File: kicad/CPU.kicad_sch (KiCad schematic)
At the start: 24 parts, among them U12 GAL22V10, U16 74LS245, U17 74LS244, U18 74LS244, U19 74LS244, U20 74LS245, U3 68010P10, U4 GAL22V10, U5 SST39SF040, U6 AS6C4008-55PCN, U7 SST39SF040, U8 AS6C4008-55PCN

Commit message: Added Bus error handling
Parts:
- added J3, J4: Conn_01x01_Pin, symbol Connector:Conn_01x01_Pin
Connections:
- net at U4.1 (I0/CLK): now also J4.1 (Pin_1)
- net AS: now reaches U4.22 (I/O)
- net at U4.23 (I/O): now also J3.1 (Pin_1)
- net at R8.2, U3.12 (BGACK), U3.13 (BR)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: no longer U3.22 (BERR)
- net E: now reaches U3.20 (E)
- new net ~{BERR}: U3.22 (BERR)
- no-connect marks 22 -> 18
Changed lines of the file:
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@@
   (junction (at 275.59 25.4) (diameter 0) (color 0 0 0 0)
   )
-  (junction (at 20.32 88.9) (diameter 0) (color 0 0 0 0)
-  )
   (junction (at 265.43 236.22) (diameter 0) (color 0 0 0 0)
   )
@@
   )
   (no_connect (at 146.05 151.13))
-  (no_connect (at 40.64 77.47))
   (no_connect (at 237.49 90.17))
   (no_connect (at 212.09 87.63))
@@
   (no_connect (at 212.09 69.85))
   (no_connect (at 40.64 74.93))
-  (no_connect (at 238.76 163.83))
   (no_connect (at 237.49 77.47))
   (no_connect (at 171.45 151.13))
@@
   (no_connect (at 212.09 85.09))
   (no_connect (at 40.64 52.07))
-  (no_connect (at 213.36 161.29))
   (no_connect (at 237.49 67.31))
   (no_connect (at 237.49 72.39))
   (no_connect (at 237.49 64.77))
   (no_connect (at 237.49 69.85))
-  (no_connect (at 238.76 166.37))
   (bus_entry (at 275.59 57.15) (size 2.54 2.54)
     (stroke (width 0) (type default))
@@
     (stroke (width 0) (type default))
   )
-  (wire (pts (xy 35.56 102.87) (xy 35.56 88.9))
-    (stroke (width 0) (type default))
-  )
   (wire (pts (xy 332.74 87.63) (xy 347.98 87.63))
     (stroke (width 0) (type default))
@@
     (stroke (width 0) (type default))
   )
+  (wire (pts (xy 212.09 151.13) (xy 213.36 151.13))
+    (stroke (width 0) (type default))
+  )
   (wire (pts (xy 278.13 191.77) (xy 292.1 191.77))
     (stroke (width 0) (type default))
@@
     (stroke (width 0) (type default))
   )
+  (wire (pts (xy 250.19 151.13) (xy 250.19 163.83))
+    (stroke (width 0) (type default))
+  )
   (bus (pts (xy 101.6 102.87) (xy 101.6 105.41))
     (stroke (width 0) (type default))
@@
     (stroke (width 0) (type default))
   )
+  (wire (pts (xy 238.76 163.83) (xy 250.19 163.83))
+    (stroke (width 0) (type default))
+  )
   (wire (pts (xy 171.45 91.44) (xy 180.34 91.44))
     (stroke (width 0) (type default))
@@
     (stroke (width 0) (type default))
   )
+  (wire (pts (xy 248.92 151.13) (xy 250.19 151.13))
+    (stroke (width 0) (type default))
+  )
   (bus (pts (xy 275.59 87.63) (xy 275.59 90.17))
     (stroke (width 0) (type default))
@@
     (stroke (width 0) (type default))
   )
+  (wire (pts (xy 213.36 161.29) (xy 213.36 151.13))
+    (stroke (width 0) (type default))
+  )
   (wire (pts (xy 335.28 204.47) (xy 350.52 204.47))
     (stroke (width 0) (type default))
@@
     (stroke (width 0) (type default))
   )
-  (wire (pts (xy 20.32 80.01) (xy 20.32 88.9))
+  (wire (pts (xy 20.32 80.01) (xy 20.32 90.17))
     (stroke (width 0) (type default))
   )
@@
     (stroke (width 0) (type default))
   )
-  (wire (pts (xy 35.56 88.9) (xy 20.32 88.9))
-    (stroke (width 0) (type default))
-  )
   (bus (pts (xy 275.59 201.93) (xy 275.59 204.47))
     (stroke (width 0) (type default))
@@
     (stroke (width 0) (type default))
   )
-  (wire (pts (xy 40.64 102.87) (xy 35.56 102.87))
-    (stroke (width 0) (type default))
-  )
   (bus (pts (xy 182.88 29.21) (xy 182.88 25.4))
     (stroke (width 0) (type default))
@@
     (stroke (width 0) (type default))
   )
-  (wire (pts (xy 20.32 88.9) (xy 20.32 90.17))
-    (stroke (width 0) (type default))
-  )
   (bus (pts (xy 129.54 130.81) (xy 129.54 133.35))
     (stroke (width 0) (type default))
@@
     (stroke (width 0) (type default))
   )
+  (wire (pts (xy 38.1 102.87) (xy 40.64 102.87))
+    (stroke (width 0) (type default))
+  )
   (wire (pts (xy 132.08 31.75) (xy 146.05 31.75))
     (stroke (width 0) (type default))
@@
     )
   )
+  (global_label "AS" (shape output) (at 238.76 166.37 0) (fields_autoplaced)
+    (effects (font (size 1.27 1.27)) (justify left))
+    (property "Intersheetrefs" "${INTERSHEET_REFS}" (at 243.9639 166.37 0)
+      (effects (font (size 1.27 1.27)) (justify left) hide)
+    )
+  )
   (global_label "~{ROMSEL}" (shape output) (at 238.76 184.15 0) (fields_autoplaced)
     (effects (font (size 1.27 1.27)) (justify left))
@@
     )
   )
+  (global_label "~{BERR}" (shape input) (at 38.1 102.87 180) (fields_autoplaced)
+    (effects (font (size 1.27 1.27)) (justify right))
+    (property "Intersheetrefs" "${INTERSHEET_REFS}" (at 30.2352 102.87 0)
+      (effects (font (size 1.27 1.27)) (justify right) hide)
+    )
+  )
   (global_label "A18" (shape output) (at 109.22 74.93 0) (fields_autoplaced)
     (effects (font (size 1.27 1.27)) (justify left))
@@
     )
   )
+  (global_label "E" (shape output) (at 40.64 77.47 180) (fields_autoplaced)
+    (effects (font (size 1.27 1.27)) (justify right))
+    (property "Intersheetrefs" "${INTERSHEET_REFS}" (at 36.5852 77.47 0)
+      (effects (font (size 1.27 1.27)) (justify right) hide)
+    )
+  )
   (global_label "~{HALT}" (shape bidirectional) (at 29.21 118.11 180) (fields_autoplaced)
     (effects (font (size 1.27 1.27)) (justify right))
@@
     )
   )
+  (symbol (lib_id "Connector:Conn_01x01_Pin") (at 207.01 151.13 0) (unit 1)
+    (in_bom yes) (on_board yes) (dnp no) (fields_autoplaced)
+    (property "Reference" "J4" (at 207.645 146.05 0)
+      (effects (font (size 1.27 1.27)))
+    )
+    (property "Value" "Conn_01x01_Pin" (at 207.645 148.59 0)
+      (effects (font (size 1.27 1.27)))
+    )
+    (property "Footprint" "" (at 207.01 151.13 0)
+      (effects (font (size 1.27 1.27)) hide)
+    )
+    (property "Datasheet" "~" (at 207.01 151.13 0)
+      (effects (font (size 1.27 1.27)) hide)
+    )
+    (pin "1")
+    (instances
+      (project "mb68k"
+        (path "/e63e39d7-6ac0-4ffd-8aa3-1841a4541b55/c0b233c3-0354-40a8-9da4-8134543aeba9"
+          (reference "J4") (unit 1)
+        )
+      )
+    )
+  )
   (symbol (lib_id "74xx:74LS245") (at 158.75 195.58 0) (unit 1)
     (in_bom yes) (on_board yes) (dnp no) (fields_autoplaced)
@@
         )
       )
+    )
+  )
+  (symbol (lib_id "Connector:Conn_01x01_Pin") (at 243.84 151.13 0) (unit 1)
+    (in_bom yes) (on_board yes) (dnp no) (fields_autoplaced)
+    (property "Reference" "J3" (at 244.475 146.05 0)
+      (effects (font (size 1.27 1.27)))
+    )
+    (property "Value" "Conn_01x01_Pin" (at 244.475 148.59 0)
+      (effects (font (size 1.27 1.27)))
+    )
+    (property "Footprint" "" (at 243.84 151.13 0)
+      (effects (font (size 1.27 1.27)) hide)
+    )
+    (property "Datasheet" "~" (at 243.84 151.13 0)
+      (effects (font (size 1.27 1.27)) hide)
+    )
+    (pin "1")
+    (instances
+      (project "mb68k"
+        (path "/e63e39d7-6ac0-4ffd-8aa3-1841a4541b55/c0b233c3-0354-40a8-9da4-8134543aeba9"
+          (reference "J3") (unit 1)
+        )
+      )

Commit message: switched to GALasm
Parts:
- added C24: 100nF, Capacitor_THT:CP_Radial_D5.0mm_P2.50mm, symbol Device:C
- added J5: Conn_01x06_Pin, symbol Connector:Conn_01x06_Pin
- added J6, J7: Conn_01x01_Pin, symbol Connector:Conn_01x01_Pin
- added R32: 4k7, Resistor_THT:R_Axial_DIN0207_L6.3mm_D2.5mm_P10.16mm_Horizontal, symbol Device:R
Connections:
- net A18: no longer U4.13 (I11)
- net A19: now also U4.15 (I/O)
- net GND: now also C24.2
- net R/~{W}: now also U12.4 (I3); no longer U12.8 (I7)
- net VCC: now also C24.1, R32.1
- net _R/~{W}: now also U12.16 (I/O), U6.29 (WE#), U8.29 (WE#); no longer U12.17 (I/O)
- net ~{AS}: now also U12.2 (I1), U4.13 (I11); no longer U12.6 (I5), U4.6 (I5)
- net ~{BERR}: now also R32.2
- net ~{DTACK}: now also U4.21 (I/O)
- net ~{DUARTSEL}: now also U4.20 (I/O); no longer U4.17 (I/O)
- net ~{LDS}: now also U12.3 (I2); no longer U12.7 (I6)
- net ~{UDS}: now also U12.5 (I4); no longer U12.9 (I8)
- net ~{_LDS}: now also U12.15 (I/O); no longer U12.16 (I/O)
- net ~{_UDS}: now also U12.17 (I/O); no longer U12.15 (I/O)
- net at U12.1 (I0/CLK): now also J7.1 (Pin_1)
- net at U12.10 (I9): now also J5.2 (Pin_2)
- net at U12.11 (I10): now also J5.1 (Pin_1)
- net at U12.13 (I11): now also J6.1 (Pin_1)
- net _W/~{R}: now reaches U12.18 (I/O)
- net _W/~{R}: now also U5.24 (OE), U6.24 (OE#), U7.24 (OE), U8.24 (OE#)
- net _AS: now reaches U12.19 (I/O)
- net AS: no longer names the net of U4.22 (I/O)
- removed net ~{EVENREAD}: U4.20 (I/O), U7.24 (OE), U8.24 (OE#)
- removed net ~{EVENWRITE}: U4.21 (I/O), U8.29 (WE#)
- removed net ~{ODDREAD}: U4.18 (I/O), U5.24 (OE), U6.24 (OE#)
- net ~{ODDWRITE} renamed ~{CSEVENRAM0}
- net ~{CSEVENRAM0}: now also U8.22 (CE#); no longer U6.29 (WE#)
- removed net ~{RAM0SEL}: U4.16 (I/O), U6.22 (CE#), U8.22 (CE#)
- removed net ~{ROMSEL}: U4.15 (I/O), U5.22 (CE), U7.22 (CE)
- new net: J5.3 (Pin_3), U12.9 (I8)
- new net: J5.4 (Pin_4), U12.8 (I7)
- new net: J5.5 (Pin_5), U12.7 (I6)
- new net: J5.6 (Pin_6), U12.6 (I5)
- new net ~{CSEVENROM}: U4.17 (I/O), U7.22 (CE)
- new net ~{CSODDRAM0}: U4.18 (I/O), U6.22 (CE#)
- new net ~{CSODDROM}: U4.16 (I/O), U5.22 (CE)
- no-connect marks 18 -> 10
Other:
- note added: "Signaling"

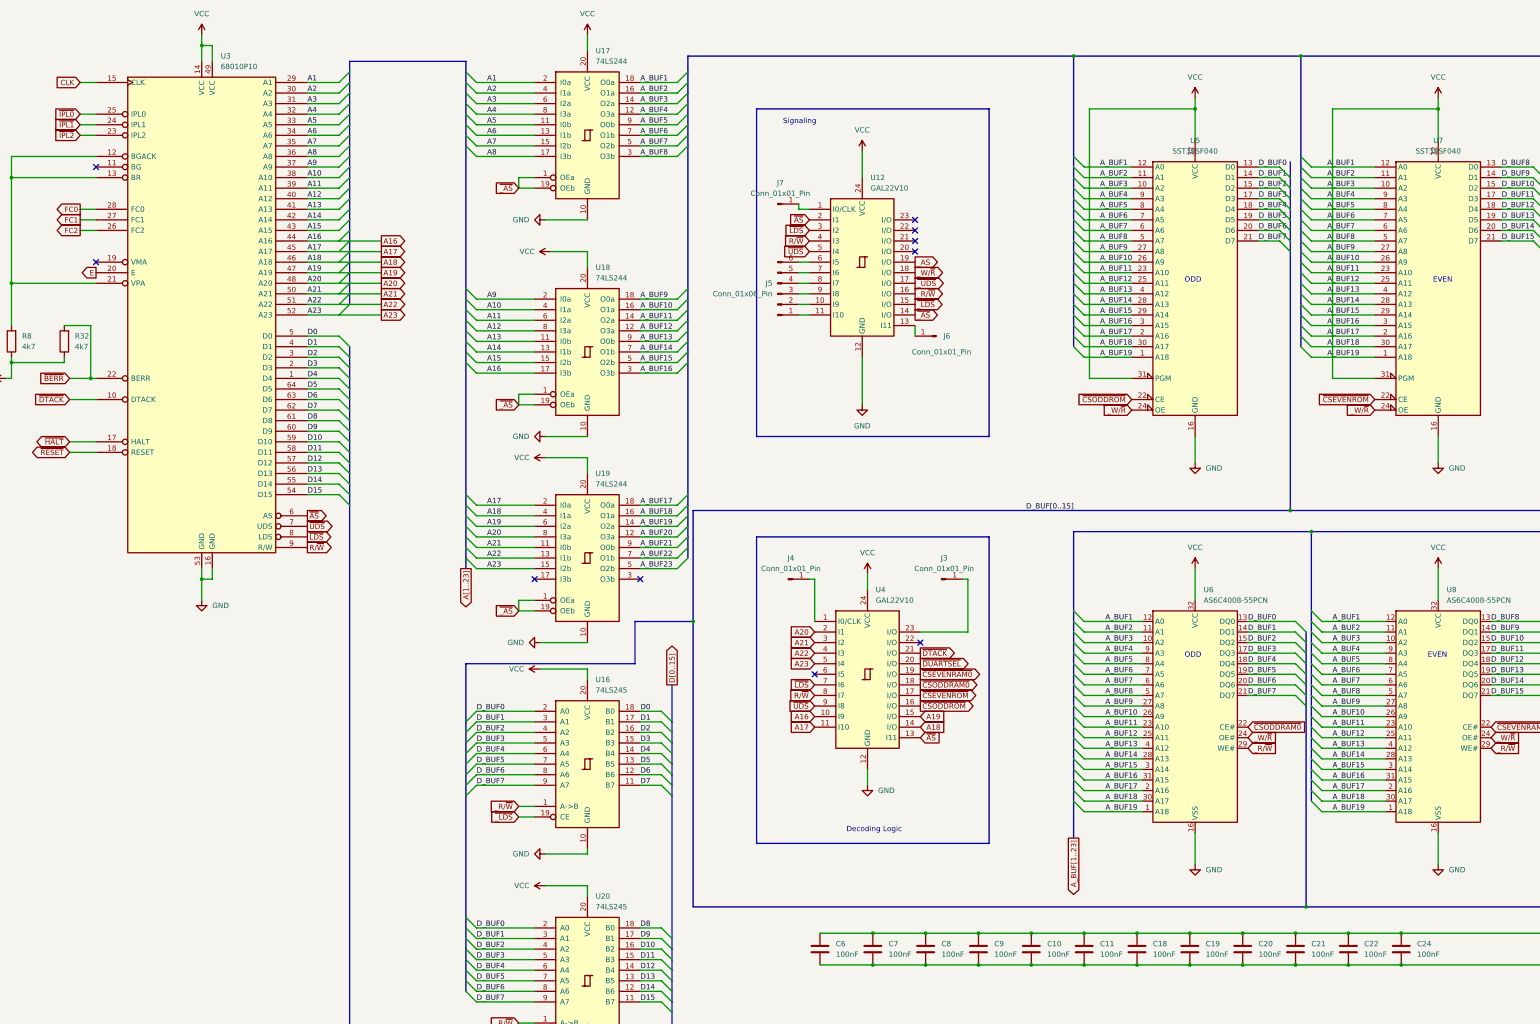
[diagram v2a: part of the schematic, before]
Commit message: added footprints
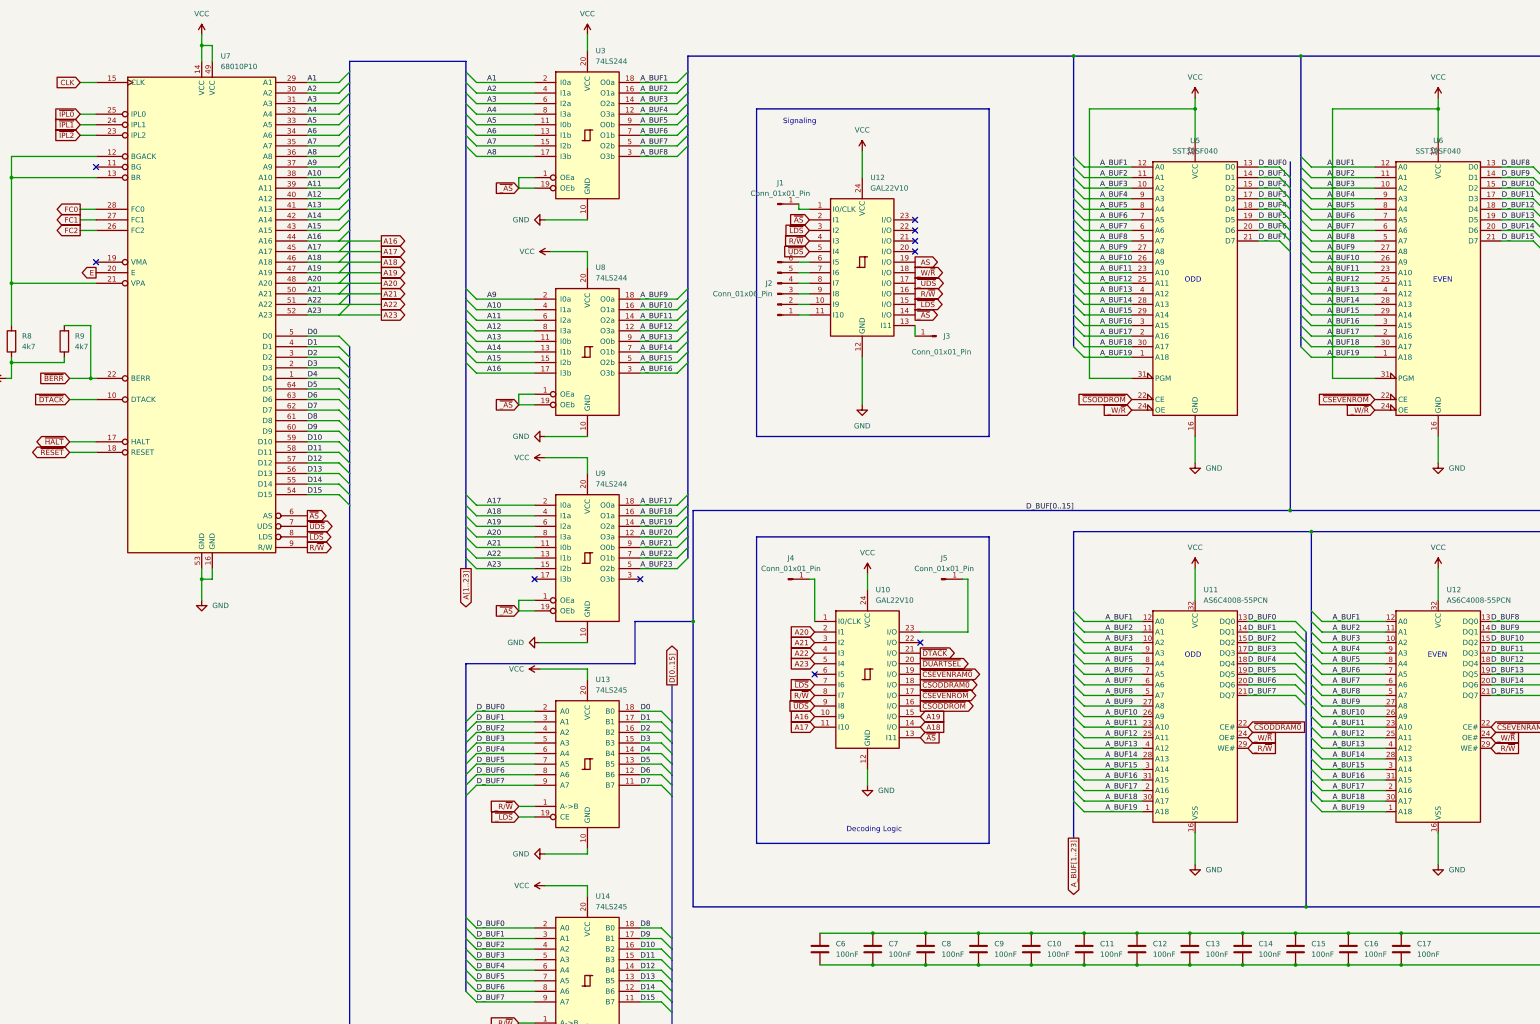
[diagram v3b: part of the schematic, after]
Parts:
- J1: renamed from J7; footprint (none) -> Connector_PinSocket_2.54mm:PinSocket_1x01_P2.54mm_Vertical
- J2: renamed from J5; footprint (none) -> Connector_PinSocket_2.54mm:PinSocket_1x06_P2.54mm_Vertical
- J3: renamed from J6; footprint (none) -> Connector_PinSocket_2.54mm:PinSocket_1x01_P2.54mm_Vertical
- J4: footprint (none) -> Connector_PinSocket_2.54mm:PinSocket_1x01_P2.54mm_Vertical
- J5: renamed from J3; footprint (none) -> Connector_PinSocket_2.54mm:PinSocket_1x01_P2.54mm_Vertical
- U10: renamed from U4; footprint (none) -> Package_DIP:DIP-24_W15.24mm_Socket
- U12: footprint (none) -> Package_DIP:DIP-24_W7.62mm_Socket
- U13: renamed from U16; footprint (none) -> Package_DIP:DIP-20_W7.62mm_Socket
- U14: renamed from U20; footprint (none) -> Package_DIP:DIP-20_W7.62mm_Socket
- U3: renamed from U17; footprint (none) -> Package_DIP:DIP-20_W7.62mm_Socket
- U7: renamed from U3; footprint matsb:MC68000-DIL64 -> Package_DIP:DIL64
- U8: renamed from U18; footprint (none) -> Package_DIP:DIP-20_W7.62mm_Socket
- U9: renamed from U19; footprint (none) -> Package_DIP:DIP-20_W7.62mm_Socket
- renumbered C18 to C12, C19 to C13, C20 to C14, C21 to C15, C22 to C16, C24 to C17, R32 to R9, U6 to U11, U8 to U12, U7 to U6

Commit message: updated readme
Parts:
- added C18: 100nF, Capacitor_THT:CP_Radial_D5.0mm_P2.50mm, symbol Device:C
- U10: footprint Package_DIP:DIP-24_W15.24mm_Socket -> Package_DIP:DIP-24_W7.62mm_Socket
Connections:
- net GND: now also C18.2
- net VCC: now also C18.1
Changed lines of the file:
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@@
   (junction (at 290.83 236.22) (diameter 0) (color 0 0 0 0)
   )
+  (junction (at 368.3 243.84) (diameter 0) (color 0 0 0 0)
+  )
   (junction (at 227.33 243.84) (diameter 0) (color 0 0 0 0)
   )
@@
   (junction (at 184.15 161.29) (diameter 0) (color 0 0 0 0)
   )
+  (junction (at 368.3 236.22) (diameter 0) (color 0 0 0 0)
+  )
   (junction (at 354.33 236.22) (diameter 0) (color 0 0 0 0)
   )
@@
     (stroke (width 0) (type default))
   )
-  (wire (pts (xy 354.33 236.22) (xy 392.43 236.22))
+  (wire (pts (xy 354.33 236.22) (xy 368.3 236.22))
     (stroke (width 0) (type default))
   )
@@
     (stroke (width 0) (type default))
   )
-  (wire (pts (xy 354.33 243.84) (xy 392.43 243.84))
+  (wire (pts (xy 354.33 243.84) (xy 368.3 243.84))
     (stroke (width 0) (type default))
   )
@@
     (stroke (width 0) (type default))
   )
+  (wire (pts (xy 368.3 243.84) (xy 392.43 243.84))
+    (stroke (width 0) (type default))
+  )
   (wire (pts (xy 209.55 80.01) (xy 212.09 80.01))
     (stroke (width 0) (type default))
@@
     (stroke (width 0) (type default))
   )
+  (wire (pts (xy 368.3 236.22) (xy 392.43 236.22))
+    (stroke (width 0) (type default))
+  )
   (wire (pts (xy 99.06 80.01) (xy 91.44 80.01))
     (stroke (width 0) (type default))
@@
       (effects (font (size 1.27 1.27)) (justify left))
     )
-    (property "Footprint" "Package_DIP:DIP-24_W15.24mm_Socket" (at 198.12 176.53 0)
+    (property "Footprint" "Package_DIP:DIP-24_W7.62mm_Socket" (at 198.12 176.53 0)
       (effects (font (size 1.27 1.27)) hide)
     )
@@
         )
       )
+    )
+  )
+  (symbol (lib_id "Device:C") (at 368.3 240.03 0) (unit 1)
+    (in_bom yes) (on_board yes) (dnp no) (fields_autoplaced)
+    (property "Reference" "C18" (at 372.11 238.7599 0)
+      (effects (font (size 1.27 1.27)) (justify left))
+    )
+    (property "Value" "100nF" (at 372.11 241.2999 0)
+      (effects (font (size 1.27 1.27)) (justify left))
+    )
+    (property "Footprint" "Capacitor_THT:CP_Radial_D5.0mm_P2.50mm" (at 369.2652 243.84 0)
+      (effects (font (size 1.27 1.27)) hide)
+    )
+    (property "Datasheet" "~" (at 368.3 240.03 0)
+      (effects (font (size 1.27 1.27)) hide)
+    )
+    (pin "1")
+    (pin "2")
+    (instances
+      (project "mb68k"
+        (path "/e63e39d7-6ac0-4ffd-8aa3-1841a4541b55/c0b233c3-0354-40a8-9da4-8134543aeba9"
+          (reference "C18") (unit 1)
+        )
+      )
